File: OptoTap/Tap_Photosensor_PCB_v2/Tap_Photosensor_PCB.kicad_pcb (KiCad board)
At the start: 2 copper layers, 28.8 x 14.3 mm, 12 parts, among them J1 Conn_01x03, U1 OPB961N51, U2 AP63205WU

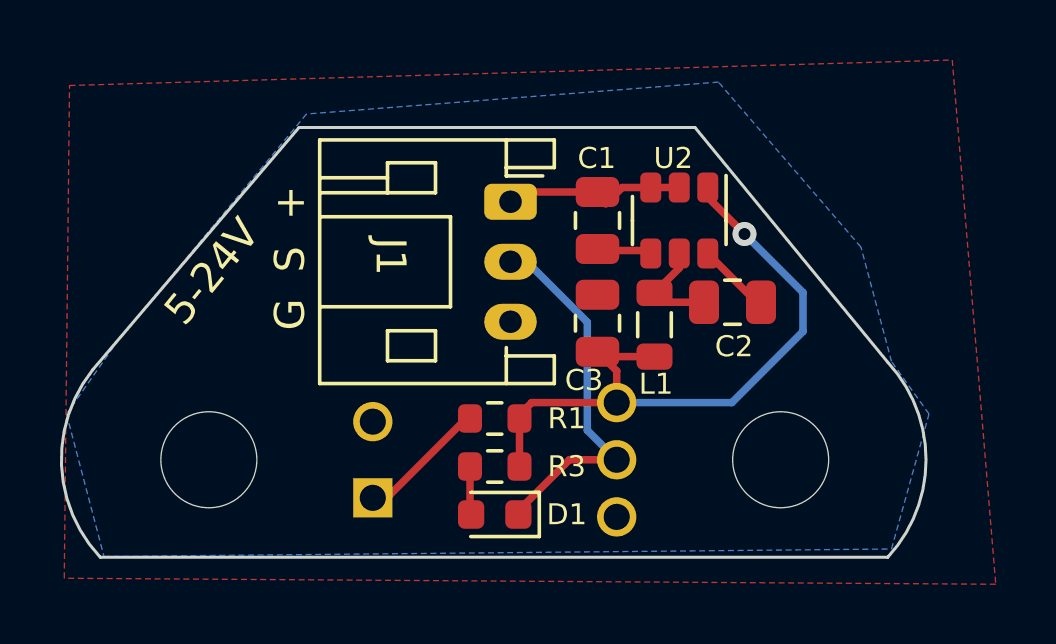
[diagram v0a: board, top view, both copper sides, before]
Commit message: updated OptoTap boards (#53)
* updated OptoTap boards

* changed footprint text to specify EE-SX398

* added solder jig step

* fixed link
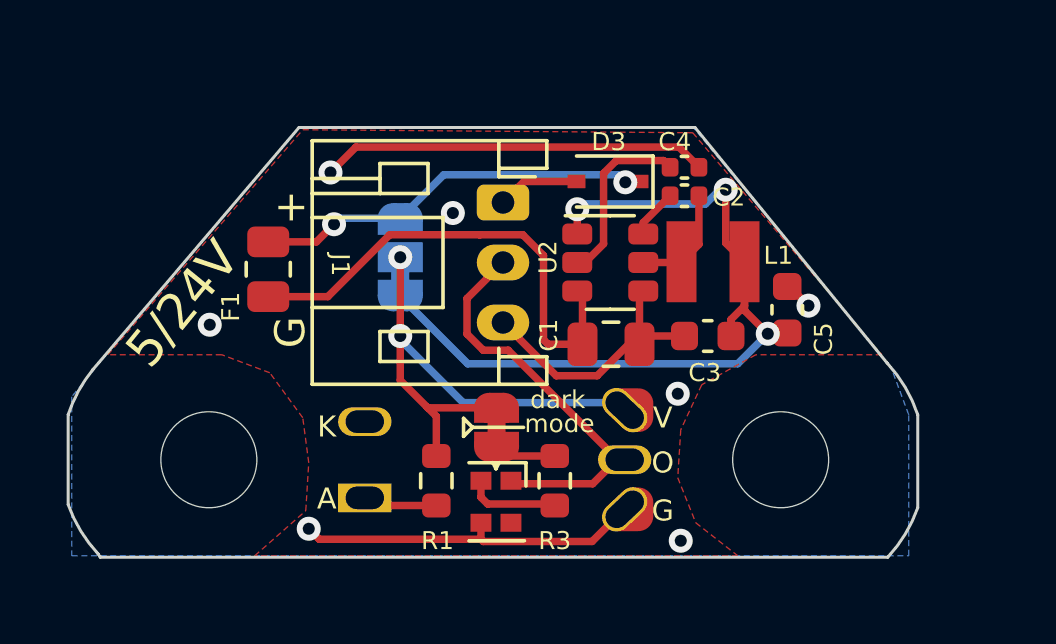
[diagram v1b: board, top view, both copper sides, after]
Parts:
- added C4: 68 nF, Capacitor_SMD:C_0402_1005Metric, F.Cu at (118.7, 55.8)
- added C5: 22 µF, Capacitor_SMD:C_0603_1608Metric, F.Cu at (122.2, 60.5)
- added D3: D_Schottky, Diode_SMD:D_SOD-323, F.Cu at (116.2, 56.2)
- added F1: Polyfuse_Small, Resistor_SMD:R_0805_2012Metric, F.Cu at (104.8, 59.1)
- added JP1: SolderJumper_3_Bridged12, Jumper:SolderJumper-3_P1.3mm_Bridged12_RoundedPad1.0x1.5mm_NumberLabels, B.Cu at (109.2, 58.8)
- added JP2: SolderJumper_2_Bridged, Jumper:SolderJumper-2_DARKMODE, F.Cu at (112.5, 64.4)
- C2: value 220 nF -> 100 nF; footprint Capacitor_SMD:C_0805_2012Metric -> Capacitor_SMD:C_0402_1005Metric
- C3: footprint Capacitor_SMD:C_0805_2012Metric -> Capacitor_SMD:C_0603_1608Metric
- D1: value LED -> XL-1615RGBC; footprint LED_SMD:LED_0603_1608Metric -> LED_SMD:LED_0606_1432
- L1: footprint Inductor_SMD:L_0805_2012Metric -> Inductor_SMD:CKCS3010
- R3: value 640R -> 620R
- U1: footprint footprints:OPTO_OPB961N51 -> footprints:OPTO_EE-SX398_OPB666N
- moved C1 4.15 mm to (116.3, 61.6), turned to 0 degrees
- moved C2 3.89 mm to (118.7, 56.7), turned to 180 degrees
- moved C3 3.70 mm to (119.5, 61.4), turned to 180 degrees
- moved L1 2.87 mm to (119.7, 58.9), turned to 0 degrees
- moved R1 2.85 mm to (110.5, 66.2), turned to -90 degrees
- moved U2 2.69 mm to (116.2, 58.9), turned to 0 degrees
- moved R3 2.06 mm to (114.4, 66.2), turned to -90 degrees
- moved D1 0.43 mm to (112.4, 66.9), turned to -90 degrees
- moved J1 0.25 mm to (112.7, 56.9)
- turned U1 to 180 degrees
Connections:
- net Net-(C2-Pad1) renamed /sw_node
- net Net-(C2-Pad2) renamed /bst
- C1 pad 1: Vin -> /fuse_out
- C3 pad 1: +5V -> /fb
- L1 pad 2: +5V -> /fb
- R3 pad 1: +5V -> Net-(JP2-A)
- U2 pad 1: +5V -> /fb
- U2 pad 2: Vin -> Net-(U2-EN)
- U2 pad 3: Vin -> /fuse_out
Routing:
- net GND: track 1.95 -> 35.8 mm, vias 0 -> 7
- net /fb: track 0.00 -> 27.7 mm, vias 0 -> 3
- net /fuse_out: track 0.00 -> 16.3 mm
- net Vcc: track 0.00 -> 13.4 mm, vias 0 -> 2
- net Net-(U2-EN): track 0.00 -> 5.97 mm
- net +5V: track 22.2 -> 17.6 mm, vias 1 -> 2
- net Vin: track 5.77 -> 2.74 mm
- net Net-(U1-ANODE): track 4.39 -> 2.22 mm
- net Net-(JP2-A): track 0.00 -> 2.07 mm
- net Net-(D1-A): track 1.62 -> 3.12 mm
- net SIG: track 12.4 -> 13.5 mm
- net /bst: track 2.45 -> 1.65 mm
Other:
- board size 28.8 x 14.3 mm -> 28.3 x 14.3 mm
- board text added: "5/24V"
- board text added: "5V 24V"
- board text added: "G +"
- board text added: "OptoTap"
- board text added: "cut trace to change"
- board text added: "rev 2.4.1"
- board text removed: "5-24V"
- board text removed: "5-24V OK"
- board text removed: "G S +"
- board text removed: "OPB666N"
- board text removed: "OptoTap PCB"
- board text removed: "rev 2.1"

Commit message: Opto24 (#68)
* updated OptoTap boards

* updated inductor info

* updated STEP and kicad

* updated README with LED ordering info

* fixed bad save
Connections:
- net Net-(D1-A) renamed /LED+
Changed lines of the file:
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@@
   (net 8 "/bst")
   (net 9 "/fb")
-  (net 10 "Net-(D1-A)")
+  (net 10 "/LED+")
   (net 11 "Vcc")
   (net 12 "unconnected-(D1-G-Pad4)")
@@
     (property "ki_description" "Generic connector, single row, 01x03, script generated (kicad-library-utils/schlib/autogen/connector/)")
     (property "ki_keywords" "connector")
-    (attr through_hole exclude_from_pos_files exclude_from_bom)
+    (attr through_hole exclude_from_pos_files)
     (fp_text reference "J1" (at 2.075 5.425 -90 unlocked) (layer "F.SilkS")
         (effects (font (size 0.6 0.6) (thickness 0.1)))
@@
     (property "ki_description" "Solder Jumper, 2-pole, closed/bridged")
     (property "ki_keywords" "solder jumper SPST")
-    (attr exclude_from_pos_files exclude_from_bom)
+    (attr exclude_from_pos_files)
     (net_tie_pad_groups "1, 2")
     (fp_text reference "JP2" (at 0.05 -2.5) (layer "F.SilkS") hide
@@
       (net 1 "SIG") (pinfunction "R") (pintype "input"))
     (pad "2" smd rect (at -0.7 0.5 270) (size 0.6 0.7) (layers "F.Cu" "F.Paste" "F.Mask")
-      (net 10 "Net-(D1-A)") (pinfunction "A") (pintype "power_in"))
+      (net 10 "/LED+") (pinfunction "A") (pintype "power_in"))
     (pad "3" smd rect (at 0.7 0.5 270) (size 0.6 0.7) (layers "F.Cu" "F.Paste" "F.Mask")
       (net 2 "GND") (pinfunction "B") (pintype "input"))
@@
       (net 13 "Net-(JP2-A)") (pintype "passive"))
     (pad "2" smd roundrect (at 0.825 0 270) (size 0.8 0.95) (layers "F.Cu" "F.Paste" "F.Mask") (roundrect_rratio 0.25)
-      (net 10 "Net-(D1-A)") (pintype "passive"))
+      (net 10 "/LED+") (pintype "passive"))
     (model "${KICAD6_3DMODEL_DIR}/Resistor_SMD.3dshapes/R_0603_1608Metric.wrl"
       (offset (xyz 0 0 0))
@@
     (property "Sheetfile" "Tap_Photosensor_PCB.kicad_sch")
     (property "Sheetname" "")
-    (attr through_hole exclude_from_pos_files exclude_from_bom)
+    (attr through_hole exclude_from_pos_files)
     (fp_text reference "U1" (at 7.5 2.5) (layer "B.SilkS")
         (effects (font (size 1 1) (thickness 0.15)) (justify mirror))
@@
     (property "ki_description" "3-pole Solder Jumper, pins 1+2 closed/bridged")
     (property "ki_keywords" "Solder Jumper SPDT")
-    (attr exclude_from_pos_files exclude_from_bom)
+    (attr exclude_from_pos_files)
     (net_tie_pad_groups "1, 2, 3")
     (fp_text reference "JP1" (at 0 2.25 90) (layer "B.SilkS") hide
